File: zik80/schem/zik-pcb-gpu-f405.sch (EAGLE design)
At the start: 14 parts

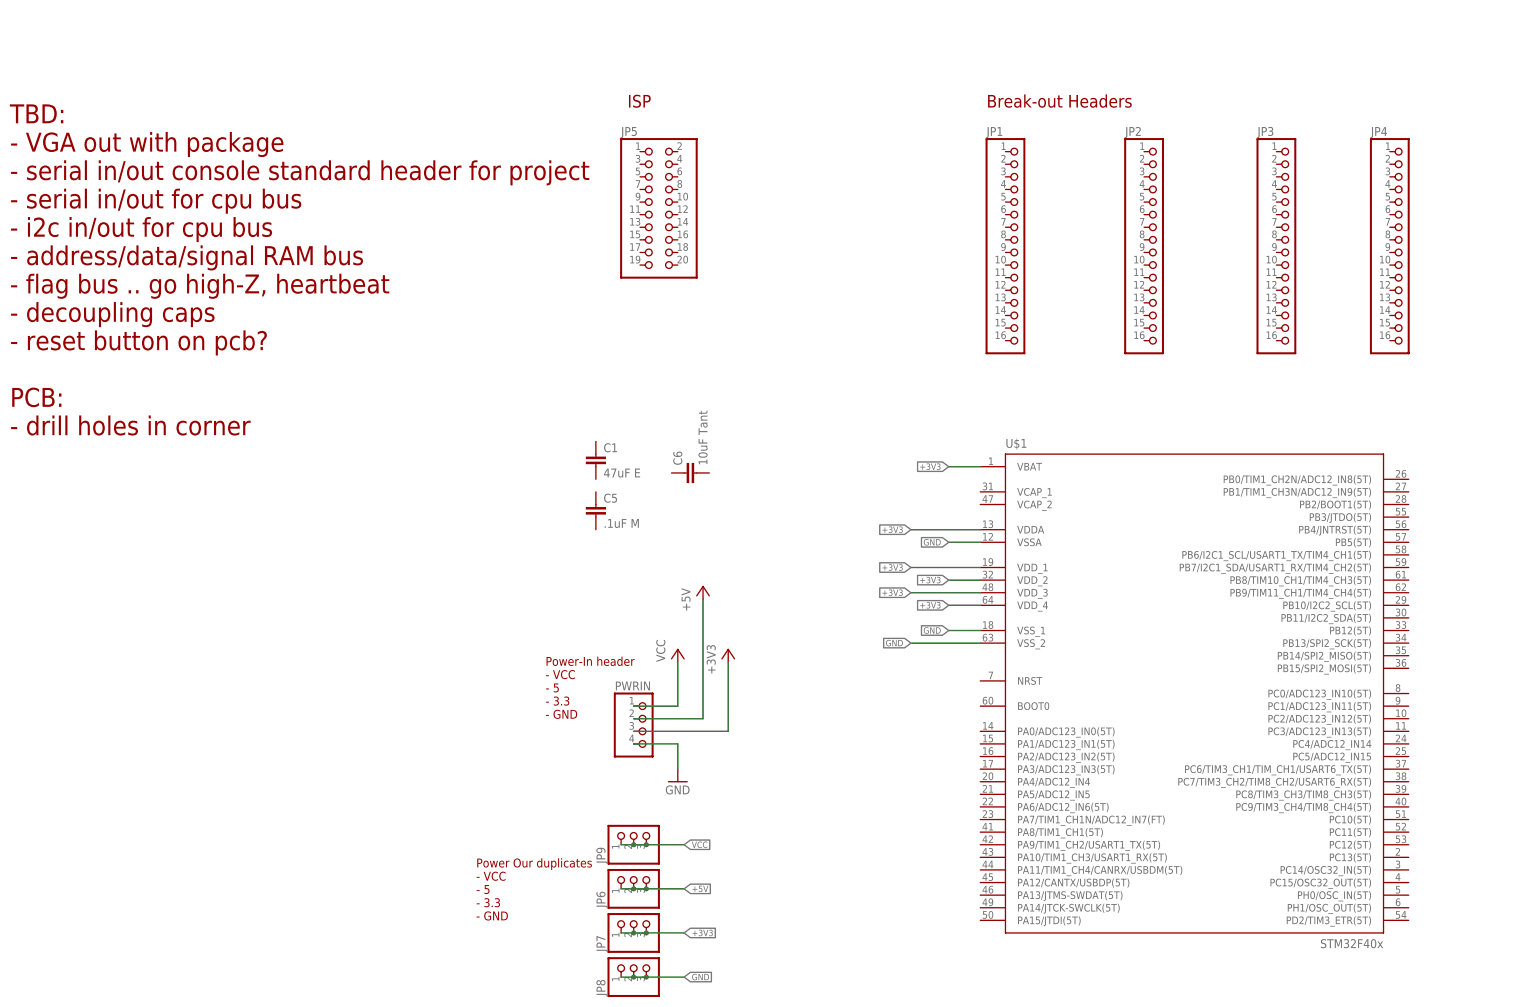
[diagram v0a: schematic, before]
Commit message: Updating schem for gpu
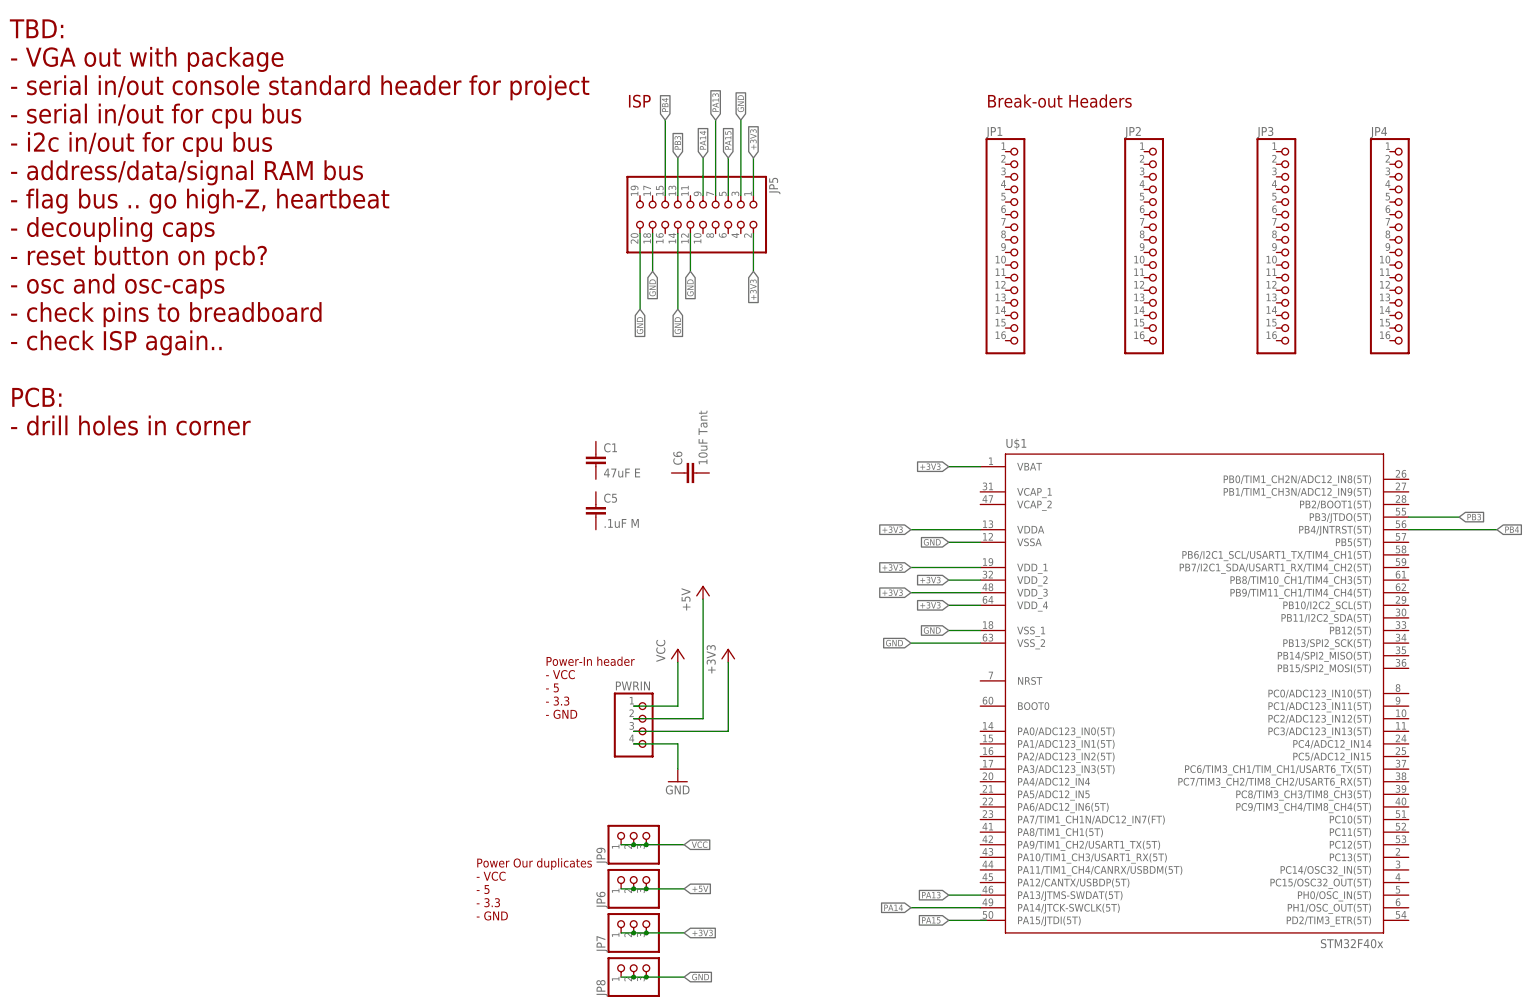
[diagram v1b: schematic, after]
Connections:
- new net PA13: JP5.7, U$1.PA13/JTMS-SWDAT(5T)
- new net PA14: JP5.9, U$1.PA14/JTCK-SWCLK(5T)
- new net PA15: JP5.5
- new net PB3: JP5.13, U$1.PB3/JTDO(5T)
- new net PB4: JP5.15, U$1.PB4/JNTRST(5T)
- net +3V3: now also JP5.1, JP5.2
- net GND: now also JP5.12, JP5.14, JP5.18, JP5.20, JP5.3
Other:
- note added: "TBD: - VGA out with package - serial in/out console standard header for project - serial in/out for cpu bus - i2c in/out for cpu bus - address/data/signal RAM bus - flag bus .. go high-Z, heartbeat - decoupling caps - reset button on pcb? - osc and osc-caps - check pins to breadboard - check ISP again.. PCB: - drill holes in corner"
- note removed: "TBD: - VGA out with package - serial in/out console standard header for project - serial in/out for cpu bus - i2c in/out for cpu bus - address/data/signal RAM bus - flag bus .. go high-Z, heartbeat - decoupling caps - reset button on pcb? PCB: - drill holes in corner"
- moved on the sheet: JP5
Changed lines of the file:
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@@
 - decoupling caps
 - reset button on pcb?
+- osc and osc-caps
+- check pins to breadboard
+- check ISP again..
 PCB:
 - drill holes in corner</text>
@@
 <instance part="JP4" gate="A" x="158.75" y="104.14"/>
 <instance part="P+1" gate="VCC" x="12.7" y="21.59"/>
-<instance part="JP5" gate="A" x="7.62" y="111.76"/>
+<instance part="JP5" gate="A" x="17.78" y="110.49" rot="R270"/>
 <instance part="JP6" gate="A" x="3.81" y="-24.13" rot="R90"/>
 <instance part="JP7" gate="A" x="3.81" y="-33.02" rot="R90"/>
@@
 <junction x="3.81" y="-35.56"/>
 </segment>
+<segment>
+<pinref part="JP5" gate="A" pin="1"/>
+<wire x1="27.94" y1="113.03" x2="27.94" y2="120.65" width="0.1524" layer="91"/>
+<label x="27.94" y="120.65" size="1.27" layer="95" rot="R90" xref="yes"/>
+</segment>
+<segment>
+<pinref part="JP5" gate="A" pin="2"/>
+<wire x1="27.94" y1="105.41" x2="27.94" y2="97.79" width="0.1524" layer="91"/>
+<label x="27.94" y="97.79" size="1.27" layer="95" rot="R270" xref="yes"/>
+</segment>
 </net>
 <net name="GND" class="0">
@@
 <junction x="6.35" y="-44.45"/>
 </segment>
-</net>
+<segment>
+<pinref part="JP5" gate="A" pin="3"/>
+<wire x1="25.4" y1="113.03" x2="25.4" y2="128.27" width="0.1524" layer="91"/>
+<label x="25.4" y="128.27" size="1.27" layer="95" rot="R90" xref="yes"/>
+</segment>
+<segment>
+<pinref part="JP5" gate="A" pin="12"/>
+<wire x1="15.24" y1="105.41" x2="15.24" y2="97.79" width="0.1524" layer="91"/>
+<label x="15.24" y="97.79" size="1.27" layer="95" rot="R270" xref="yes"/>
+</segment>
+<segment>
+<pinref part="JP5" gate="A" pin="14"/>
+<wire x1="12.7" y1="105.41" x2="12.7" y2="90.17" width="0.1524" layer="91"/>
+<label x="12.7" y="90.17" size="1.27" layer="95" rot="R270" xref="yes"/>
+</segment>
+<segment>
+<pinref part="JP5" gate="A" pin="18"/>
+<wire x1="7.62" y1="105.41" x2="7.62" y2="97.79" width="0.1524" layer="91"/>
+<label x="7.62" y="97.79" size="1.27" layer="95" rot="R270" xref="yes"/>
+</segment>
+<segment>
+<pinref part="JP5" gate="A" pin="20"/>
+<wire x1="5.08" y1="105.41" x2="5.08" y2="90.17" width="0.1524" layer="91"/>
+<label x="5.08" y="90.17" size="1.27" layer="95" rot="R270" xref="yes"/>
+</segment>
+</net>
+<net name="PA15" class="0">
+<segment>
+<wire x1="74.93" y1="-33.02" x2="67.31" y2="-33.02" width="0.1524" layer="91"/>
+<label x="67.31" y="-33.02" size="1.27" layer="95" rot="R180" xref="yes"/>
+</segment>
+<segment>
+<pinref part="JP5" gate="A" pin="5"/>
+<wire x1="22.86" y1="113.03" x2="22.86" y2="120.65" width="0.1524" layer="91"/>
+<label x="22.86" y="120.65" size="1.27" layer="95" rot="R90" xref="yes"/>
+</segment>
+</net>
+<net name="PA14" class="0">
+<segment>
+<pinref part="U$1" gate="G$1" pin="PA14/JTCK-SWCLK(5T)"/>
+<wire x1="73.66" y1="-30.48" x2="59.69" y2="-30.48" width="0.1524" layer="91"/>
+<label x="59.69" y="-30.48" size="1.27" layer="95" rot="R180" xref="yes"/>
+</segment>
+<segment>
+<pinref part="JP5" gate="A" pin="9"/>
+<wire x1="17.78" y1="113.03" x2="17.78" y2="120.65" width="0.1524" layer="91"/>
+<label x="17.78" y="120.65" size="1.27" layer="95" rot="R90" xref="yes"/>
+</segment>
+</net>
+<net name="PA13" class="0">
+<segment>
+<pinref part="U$1" gate="G$1" pin="PA13/JTMS-SWDAT(5T)"/>
+<wire x1="73.66" y1="-27.94" x2="67.31" y2="-27.94" width="0.1524" layer="91"/>
+<label x="67.31" y="-27.94" size="1.27" layer="95" rot="R180" xref="yes"/>
+</segment>
+<segment>
+<pinref part="JP5" gate="A" pin="7"/>
+<wire x1="20.32" y1="113.03" x2="20.32" y2="128.27" width="0.1524" layer="91"/>
+<label x="20.32" y="128.27" size="1.27" layer="95" rot="R90" xref="yes"/>
+</segment>
+</net>
+<net name="PB3" class="0">
+<segment>
+<pinref part="JP5" gate="A" pin="13"/>
+<wire x1="12.7" y1="113.03" x2="12.7" y2="120.65" width="0.1524" layer="91"/>
+<label x="12.7" y="120.65" size="1.27" layer="95" rot="R90" xref="yes"/>
+</segment>
+<segment>
+<pinref part="U$1" gate="G$1" pin="PB3/JTDO(5T)"/>
+<wire x1="160.02" y1="48.26" x2="170.18" y2="48.26" width="0.1524" layer="91"/>
+<label x="170.18" y="48.26" size="1.27" layer="95" xref="yes"/>
+</segment>
+</net>
+<net name="PB4" class="0">
+<segment>
+<pinref part="JP5" gate="A" pin="15"/>
+<wire x1="10.16" y1="113.03" x2="10.16" y2="128.27" width="0.1524" layer="91"/>
+<label x="10.16" y="128.27" size="1.27" layer="95" rot="R90" xref="yes"/>
+</segment>
+<segment>
+<pinref part="U$1" gate="G$1" pin="PB4/JNTRST(5T)"/>
+<wire x1="160.02" y1="45.72" x2="177.8" y2="45.72" width="0.1524" layer="91"/>
+<label x="177.8" y="45.72" size="1.27" layer="95" xref="yes"/>
+</segment>
+</net>

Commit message: minor tweaks to gpu sche.. getting mentally ready for finishing it up, deciding what is pinheader versus actual footprints..
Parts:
- removed C1: 47uF E, rcl:C-EU025-025X050
- removed C6: 10uF Tant, rcl:C-EU025-025X050
- added C2: 22pF, rcl:C-EU025-025X050
- added GPUOSC: 8Mhz, SparkFun-FreqCtrl:CRYSTALHC49US
- C5: value .1uF M -> 22pF
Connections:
- new net N$1: C5.1, GPUOSC.1, U$1.PH1/OSC_OUT(5T)
- new net N$2: C2.1, GPUOSC.2, U$1.PH0/OSC_IN(5T)
- net GND: now also C2.2, C5.2
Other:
- note added: "TBD: - VGA out with package .. drop screws, just solder points - serial in/out console standard header for project - serial in/out for cpu bus - i2c in/out for cpu bus - address/data/signal RAM bus - flag bus .. go high-Z, heartbeat, grab bus, etc - reset button on pcb? - check pins to breadboard - check ISP again.. - LED and resistor PCB: - drill holes in corner"
- note removed: "TBD: - VGA out with package - serial in/out console standard header for project - serial in/out for cpu bus - i2c in/out for cpu bus - address/data/signal RAM bus - flag bus .. go high-Z, heartbeat - decoupling caps - reset button on pcb? - osc and osc-caps - check pins to breadboard - check ISP again.. PCB: - drill holes in corner"
- moved on the sheet: C5
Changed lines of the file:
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@@
 <layer number="101" name="Patch_Top" color="12" fill="4" visible="yes" active="yes"/>
 <layer number="102" name="Vscore" color="7" fill="1" visible="yes" active="yes"/>
+<layer number="103" name="tMap" color="7" fill="1" visible="no" active="yes"/>
 <layer number="104" name="Name" color="7" fill="1" visible="yes" active="yes"/>
+<layer number="105" name="tPlate" color="7" fill="1" visible="no" active="yes"/>
+<layer number="106" name="bPlate" color="7" fill="1" visible="no" active="yes"/>
+<layer number="107" name="Crop" color="7" fill="1" visible="no" active="yes"/>
+<layer number="108" name="tplace-old" color="10" fill="1" visible="yes" active="yes"/>
+<layer number="109" name="ref-old" color="11" fill="1" visible="yes" active="yes"/>
 <layer number="116" name="Patch_BOT" color="9" fill="4" visible="yes" active="yes"/>
 <layer number="121" name="_tsilk" color="7" fill="1" visible="yes" active="yes"/>
 <layer number="122" name="_bsilk" color="7" fill="1" visible="yes" active="yes"/>
+<layer number="125" name="_tNames" color="7" fill="1" visible="no" active="yes"/>
+<layer number="144" name="Drill_legend" color="7" fill="1" visible="no" active="yes"/>
 <layer number="151" name="HeatSink" color="7" fill="1" visible="yes" active="yes"/>
+<layer number="199" name="Contour" color="7" fill="1" visible="yes" active="yes"/>
 <layer number="200" name="200bmp" color="1" fill="10" visible="no" active="no"/>
 <layer number="201" name="201bmp" color="2" fill="1" visible="no" active="no"/>
 <layer number="202" name="202bmp" color="3" fill="1" visible="no" active="no"/>
+<layer number="203" name="203bmp" color="4" fill="10" visible="no" active="yes"/>
+<layer number="204" name="204bmp" color="5" fill="10" visible="no" active="yes"/>
+<layer number="205" name="205bmp" color="6" fill="10" visible="no" active="yes"/>
+<layer number="206" name="206bmp" color="7" fill="10" visible="no" active="yes"/>
+<layer number="207" name="207bmp" color="8" fill="10" visible="no" active="yes"/>
+<layer number="208" name="208bmp" color="9" fill="10" visible="no" active="yes"/>
+<layer number="209" name="209bmp" color="7" fill="1" visible="no" active="yes"/>
+<layer number="210" name="210bmp" color="7" fill="1" visible="no" active="yes"/>
+<layer number="211" name="211bmp" color="7" fill="1" visible="no" active="yes"/>
+<layer number="212" name="212bmp" color="7" fill="1" visible="no" active="yes"/>
+<layer number="213" name="213bmp" color="7" fill="1" visible="no" active="yes"/>
+<layer number="214" name="214bmp" color="7" fill="1" visible="no" active="yes"/>
+<layer number="215" name="215bmp" color="7" fill="1" visible="no" active="yes"/>
+<layer number="216" name="216bmp" color="7" fill="1" visible="no" active="yes"/>
+<layer number="217" name="217bmp" color="18" fill="1" visible="no" active="no"/>
+<layer number="218" name="218bmp" color="19" fill="1" visible="no" active="no"/>
+<layer number="219" name="219bmp" color="20" fill="1" visible="no" active="no"/>
+<layer number="220" name="220bmp" color="21" fill="1" visible="no" active="no"/>
+<layer number="221" name="221bmp" color="22" fill="1" visible="no" active="no"/>
+<layer number="222" name="222bmp" color="23" fill="1" visible="no" active="no"/>
+<layer number="223" name="223bmp" color="24" fill="1" visible="no" active="no"/>
+<layer number="224" name="224bmp" color="25" fill="1" visible="no" active="no"/>
 <layer number="250" name="Descript" color="3" fill="1" visible="no" active="no"/>
 <layer number="251" name="SMDround" color="12" fill="11" visible="no" active="no"/>
@@
 <part name="+3V2" library="supply1" deviceset="+3V3" device=""/>
 <part name="PWRIN" library="pinhead" deviceset="PINHD-1X4" device=""/>
-<part name="C1" library="rcl" deviceset="C-EU" device="025-025X050" value="47uF E"/>
-<part name="C5" library="rcl" deviceset="C-EU" device="025-025X050" value=".1uF M"/>
-<part name="C6" library="rcl" deviceset="C-EU" device="025-025X050" value="10uF Tant"/>
+<part name="C5" library="rcl" deviceset="C-EU" device="025-025X050" value="22pF"/>
 <part name="U$1" library="stm32f4" deviceset="STM32F405R" device=""/>
 <part name="JP1" library="pinhead" deviceset="PINHD-1X16" device=""/>
@@
 <part name="JP8" library="pinhead" deviceset="PINHD-1X3" device=""/>
 <part name="JP9" library="pinhead" deviceset="PINHD-1X3" device=""/>
+<part name="GPUOSC" library="SparkFun-FreqCtrl" deviceset="CRYSTAL" device="HC49US" value="8Mhz"/>
+<part name="GND1" library="supply1" deviceset="GND" device=""/>
+<part name="GND2" library="supply1" deviceset="GND" device=""/>
+<part name="C2" library="rcl" deviceset="C-EU" device="025-025X050" value="22pF"/>
 </parts>
 <sheets>
@@
 - 3.3
 - GND</text>
-<text x="-121.92" y="64.77" size="3.81" layer="94">TBD:
-- VGA out with package
+<text x="-134.62" y="57.15" size="3.81" layer="94">TBD:
+- VGA out with package .. drop screws, just solder points
 - serial in/out console standard header for project
 - serial in/out for cpu bus
 - i2c in/out for cpu bus
 - address/data/signal RAM bus
-- flag bus .. go high-Z, heartbeat
-- decoupling caps
+- flag bus .. go high-Z, heartbeat, grab bus, etc
 - reset button on pcb?
-- osc and osc-caps
 - check pins to breadboard
 - check ISP again..
+- LED and resistor
 PCB:
 - drill holes in corner</text>
@@
 <instance part="+3V2" gate="G$1" x="22.86" y="21.59"/>
 <instance part="PWRIN" gate="A" x="6.35" y="5.08"/>
-<instance part="C1" gate="G$1" x="-3.81" y="60.96"/>
-<instance part="C5" gate="G$1" x="-3.81" y="50.8"/>
-<instance part="C6" gate="G$1" x="13.97" y="57.15" rot="R90"/>
+<instance part="C5" gate="G$1" x="165.1" y="-49.53"/>
 <instance part="U$1" gate="G$1" x="116.84" y="12.7"/>
 <instance part="JP1" gate="A" x="81.28" y="104.14"/>
@@
 <instance part="JP8" gate="A" x="3.81" y="-41.91" rot="R90"/>
 <instance part="JP9" gate="A" x="3.81" y="-15.24" rot="R90"/>
+<instance part="GPUOSC" gate="G$1" x="172.72" y="-40.64"/>
+<instance part="GND1" gate="1" x="165.1" y="-60.96"/>
+<instance part="GND2" gate="1" x="179.07" y="-60.96"/>
+<instance part="C2" gate="G$1" x="179.07" y="-49.53"/>
 </instances>
 <busses>
@@
 <label x="5.08" y="90.17" size="1.27" layer="95" rot="R270" xref="yes"/>
 </segment>
+<segment>
+<pinref part="C5" gate="G$1" pin="2"/>
+<pinref part="GND1" gate="1" pin="GND"/>
+<wire x1="165.1" y1="-58.42" x2="165.1" y2="-54.61" width="0.1524" layer="91"/>
+</segment>
+<segment>
+<pinref part="GND2" gate="1" pin="GND"/>
+<pinref part="C2" gate="G$1" pin="2"/>
+<wire x1="179.07" y1="-58.42" x2="179.07" y2="-54.61" width="0.1524" layer="91"/>
+</segment>
 </net>
 <net name="PA15" class="0">
@@
 </segment>
 </net>
+<net name="N$1" class="0">
+<segment>
+<pinref part="U$1" gate="G$1" pin="PH1/OSC_OUT(5T)"/>
+<pinref part="GPUOSC" gate="G$1" pin="1"/>
+<wire x1="160.02" y1="-30.48" x2="170.18" y2="-30.48" width="0.1524" layer="91"/>
+<wire x1="170.18" y1="-30.48" x2="170.18" y2="-40.64" width="0.1524" layer="91"/>
+<pinref part="C5" gate="G$1" pin="1"/>
+<wire x1="170.18" y1="-40.64" x2="165.1" y2="-40.64" width="0.1524" layer="91"/>
+<wire x1="165.1" y1="-40.64" x2="165.1" y2="-46.99" width="0.1524" layer="91"/>
+<junction x="170.18" y="-40.64"/>
+</segment>
+</net>
+<net name="N$2" class="0">
+<segment>
+<pinref part="U$1" gate="G$1" pin="PH0/OSC_IN(5T)"/>
+<pinref part="GPUOSC" gate="G$1" pin="2"/>
+<wire x1="160.02" y1="-27.94" x2="175.26" y2="-27.94" width="0.1524" layer="91"/>
+<wire x1="175.26" y1="-27.94" x2="175.26" y2="-40.64" width="0.1524" layer="91"/>
+<pinref part="C2" gate="G$1" pin="1"/>
+<wire x1="179.07" y1="-46.99" x2="179.07" y2="-40.64" width="0.1524" layer="91"/>
+<wire x1="179.07" y1="-40.64" x2="175.26" y2="-40.64" width="0.1524" layer="91"/>
+<junction x="175.26" y="-40.64"/>
+</segment>
+</net>
